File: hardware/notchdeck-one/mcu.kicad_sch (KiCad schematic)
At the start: 10 parts, among them J3 SWD, J4 TC2030_NL, SW17 RESET, U1 E73-2G4M08S1C

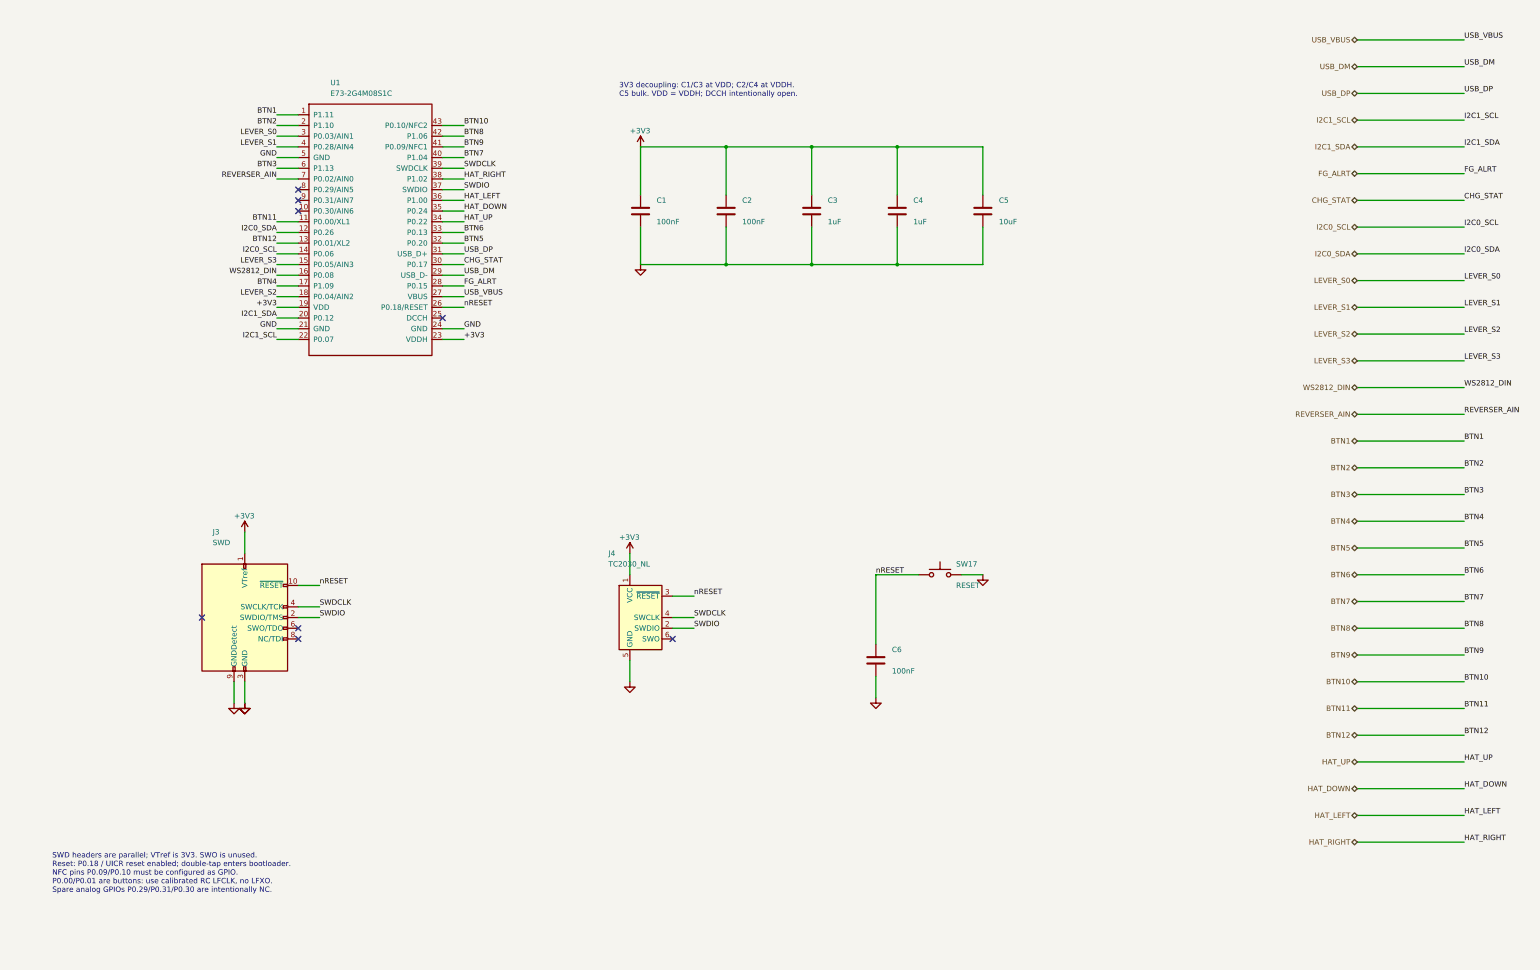
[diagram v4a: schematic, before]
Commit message: Support independent magnetic and Gray-coded power and brake handles
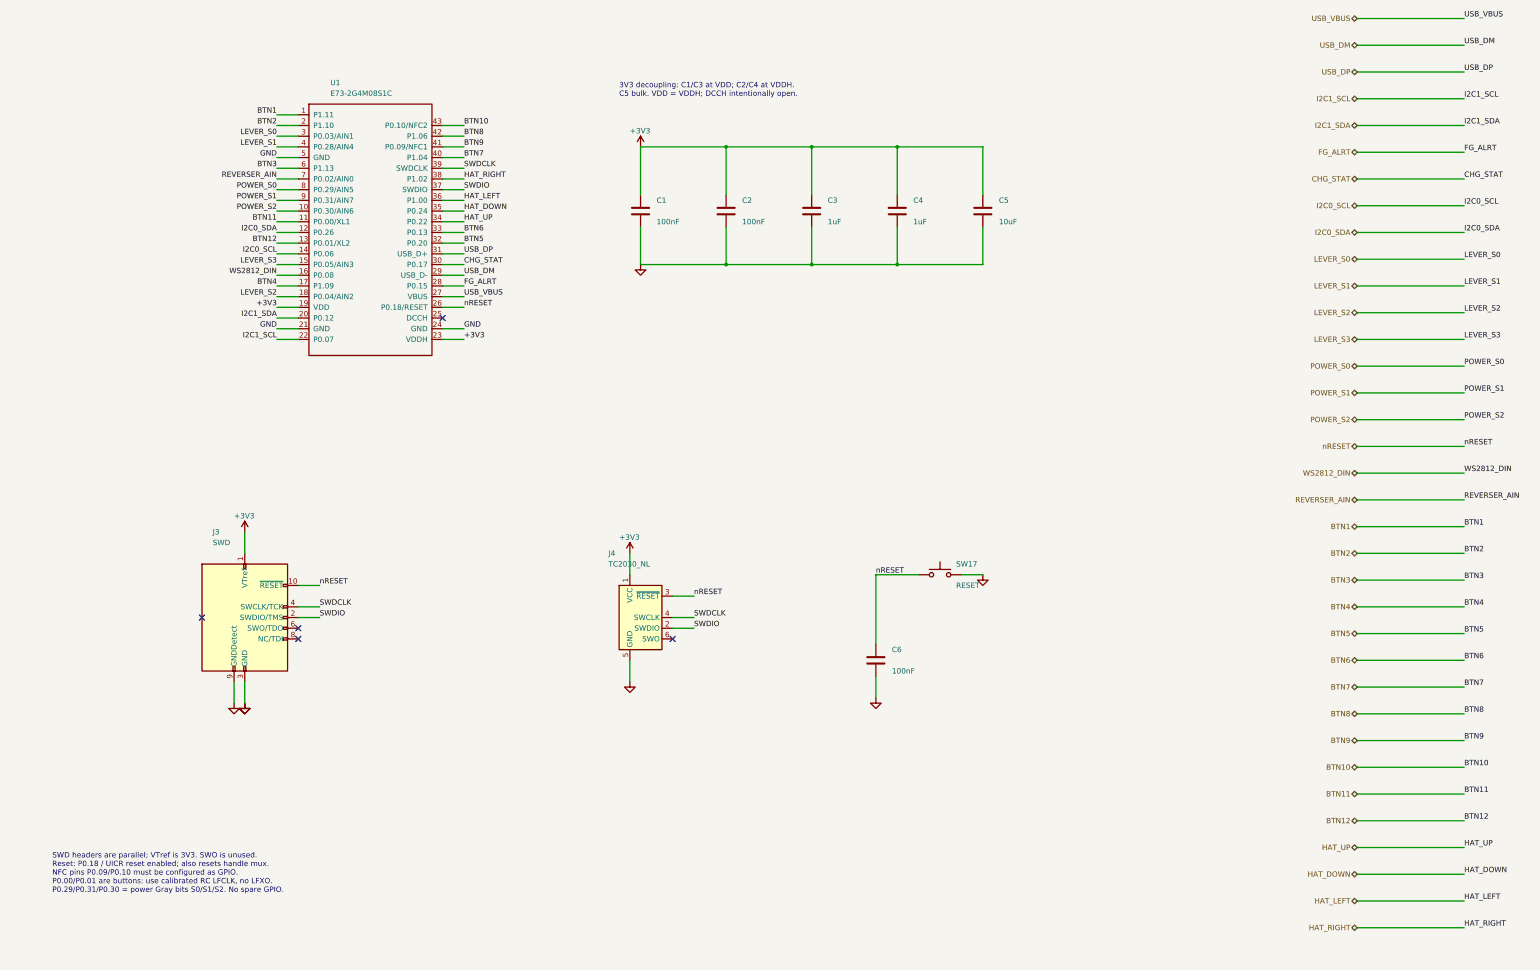
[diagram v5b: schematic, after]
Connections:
- net POWER_S2: now reaches U1.10 (P0.30/AIN6)
- net POWER_S0: now reaches U1.8 (P0.29/AIN5)
- net POWER_S1: now reaches U1.9 (P0.31/AIN7)
- no-connect marks 8 -> 5
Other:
- note added: "SWD headers are parallel; VTref is 3V3. SWO is unused. Reset: P0.18 / UICR reset enabled; also resets handle mux. NFC pins P0.09/P0.10 must be configured as GPIO. P0.00/P0.01 are buttons: use calibrated RC LFCLK, no LFXO. P0.29/P0.31/P0.30 = power Gray bits S0/S1/S2. No spare GPIO."
- note removed: "SWD headers are parallel; VTref is 3V3. SWO is unused. Reset: P0.18 / UICR reset enabled; double-tap enters bootloader. NFC pins P0.09/P0.10 must be configured as GPIO. P0.00/P0.01 are buttons: use calibrated RC LFCLK, no LFXO. Spare analog GPIOs P0.29/P0.31/P0.30 are intentionally NC."
